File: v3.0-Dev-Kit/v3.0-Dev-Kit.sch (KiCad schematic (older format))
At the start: 11 parts, among them J1 Expansion Headers, J2 Qwiic Connector, J3 NeoPixel Breakout, SW1 Up, SW2 Down, SW3 Left, SW4 Right, U1 WeMos D1 Mini, U2 SH1106 OLED

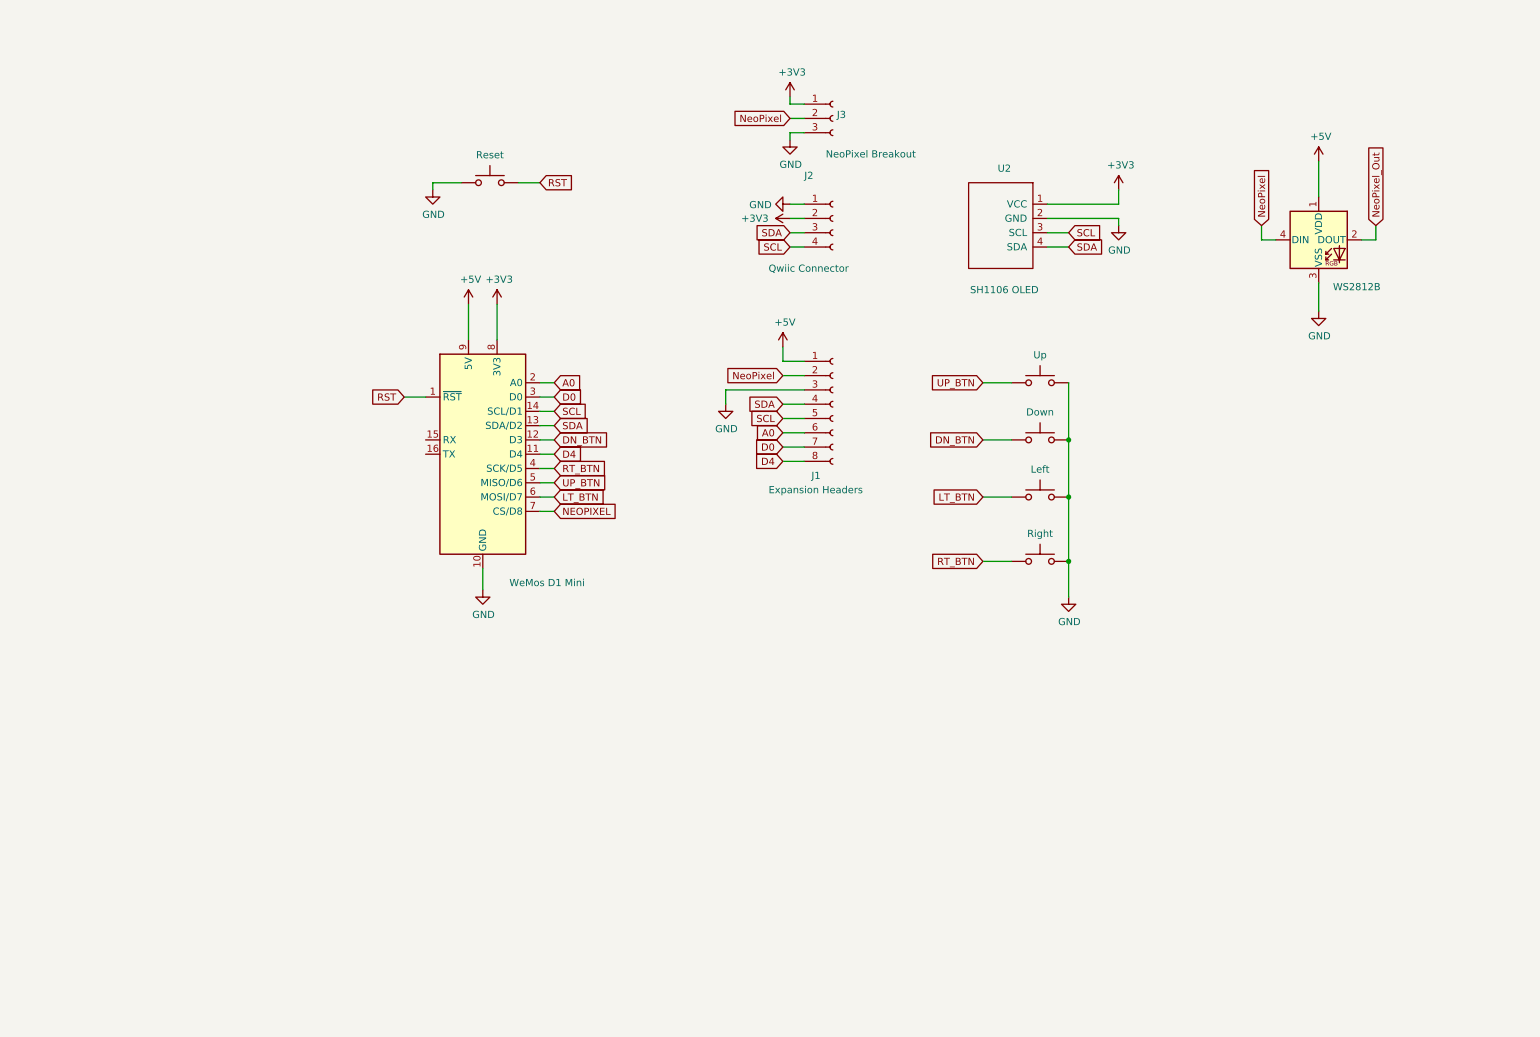
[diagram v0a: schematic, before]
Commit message: export BOM and positioning files
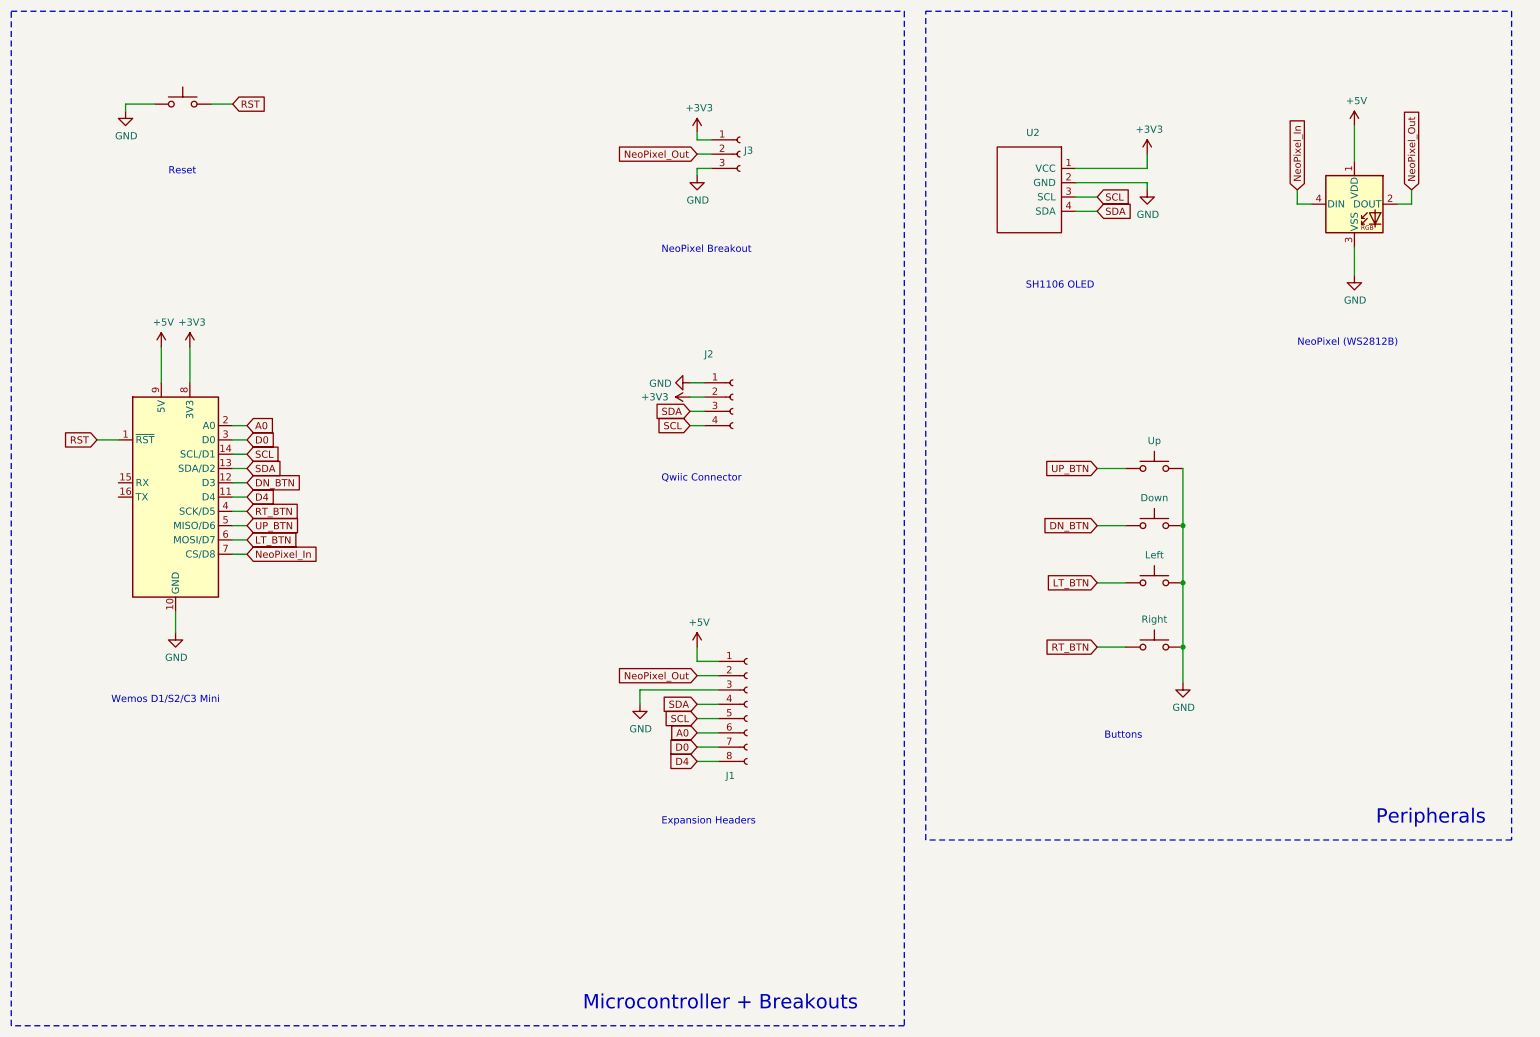
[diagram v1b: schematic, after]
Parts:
- gave numbers to parts that had none: 1
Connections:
- net NeoPixel_Out: now also J1.2 (Pin_2), J3.2 (Pin_2)
- net NEOPIXEL renamed NeoPixel_In
- net NeoPixel_In: now also D1.4 (DIN)
- removed net NeoPixel: D1.4 (DIN), J1.2 (Pin_2), J3.2 (Pin_2)
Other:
- note added: "Buttons"
- note added: "Expansion Headers"
- note added: "Microcontroller + Breakouts\n"
- note added: "NeoPixel (WS2812B)"
- note added: "NeoPixel Breakout"
- note added: "Peripherals"
- note added: "Qwiic Connector"
- note added: "Reset"
- note added: "SH1106 OLED"
- note added: "Wemos D1/S2/C3 Mini\n"
- moved on the sheet: J1, J2, J3, U2
